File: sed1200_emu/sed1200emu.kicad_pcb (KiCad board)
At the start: 2 copper layers, 114.9 x 36.2 mm, 16 parts, among them CN1 PINHD-1X6, CN2 PINHD-1X6, IC1 MEGA8-AI, Q1 CRYSTALHC49S

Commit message: Update PCB
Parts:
- moved MOSI1 45.8 mm to (153.7, 105.4)
- moved PGND2 16.6 mm to (151.8, 115.6)
- moved C3 8.52 mm to (175.3, 121.3)
- moved C4 7.65 mm to (170.8, 121.3)
- moved C1 4.02 mm to (175.9, 118.7)
- moved C2 2.01 mm to (174.0, 104.8)
- moved R6 1.42 mm to (169.5, 118.7), turned to 180 degrees
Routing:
- net VCC: track 18.2 -> 25.8 mm
- net /RS: track 27.0 -> 22.1 mm
- net Net-(C4-Pad2): track 14.8 -> 9.89 mm
- net /D0: track 38.8 -> 35.4 mm
- net Net-(DIS2-Pad3): track 3.12 -> 0.00 mm
- net Net-(C3-Pad2): track 17.0 -> 13.9 mm
- net Net-(DIS2-Pad6): track 11.2 -> 9.08 mm
- net /D2: track 32.9 -> 31.3 mm
- net /E: track 32.6 -> 31.3 mm

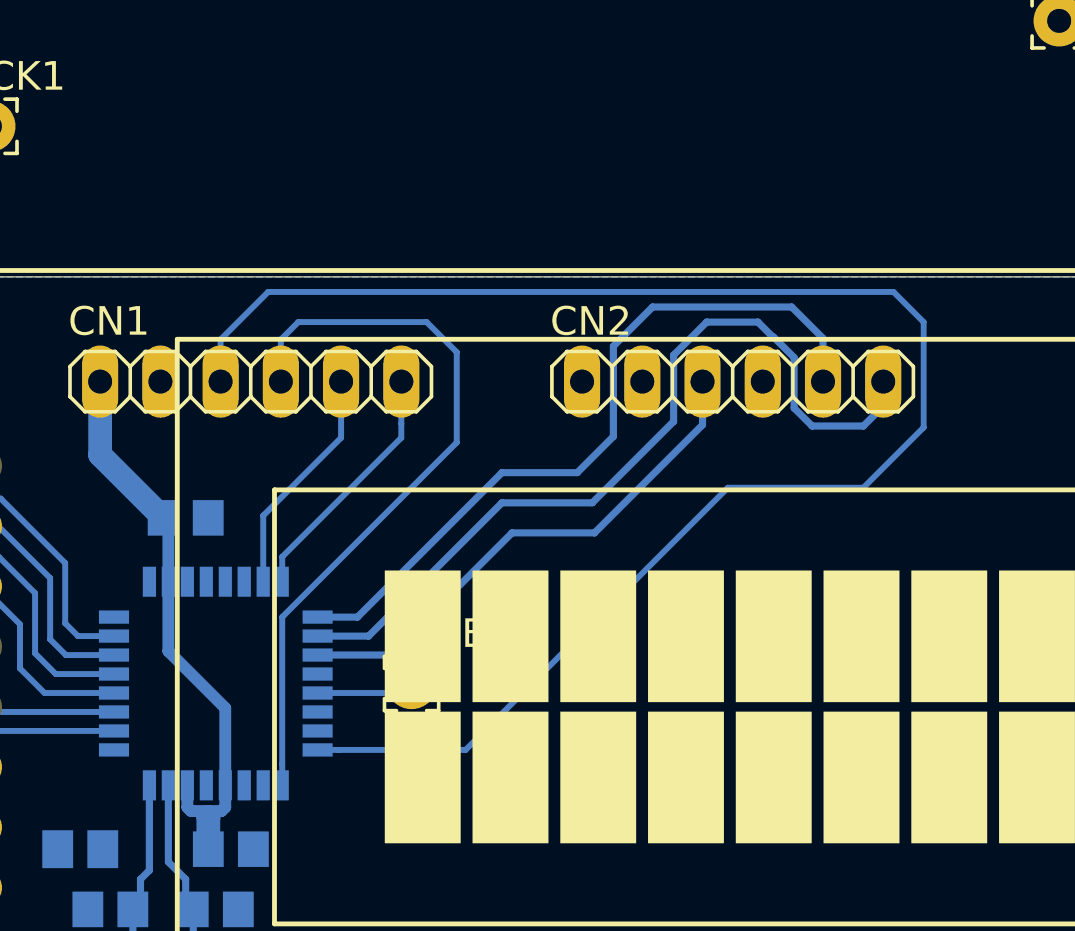
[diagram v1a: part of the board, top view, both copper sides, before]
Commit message: More SMD pads
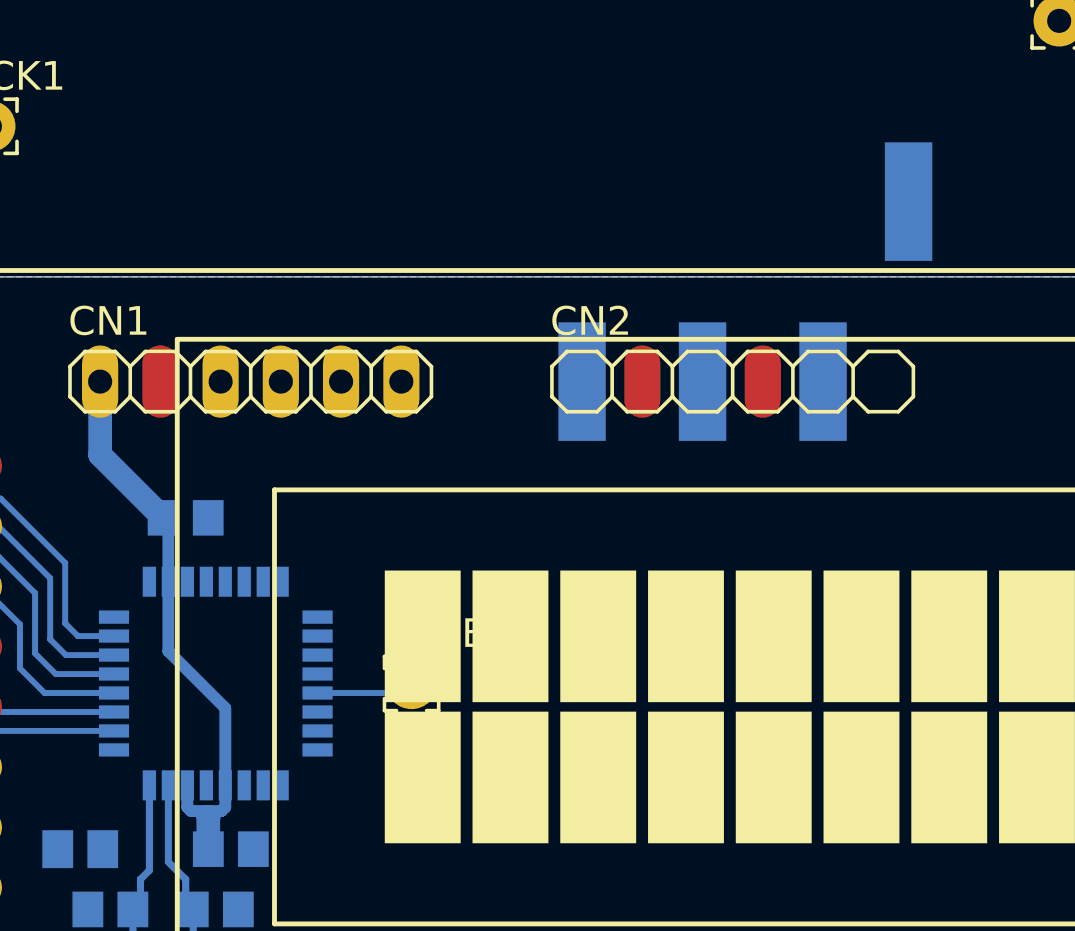
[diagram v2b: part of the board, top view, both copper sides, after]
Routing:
- net /SO_6: track 68.4 -> 0.00 mm
- net /D0: track 35.4 -> 0.00 mm
- net /E: track 31.3 -> 0.00 mm
- net /D2: track 31.3 -> 0.00 mm
- net /RS: track 22.1 -> 0.00 mm
- net /D1: track 10.5 -> 0.00 mm
- net /D3: track 9.80 -> 0.00 mm
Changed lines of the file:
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@@
     (thickness 1.6)
     (drawings 4)
-    (tracks 120)
+    (tracks 66)
     (zones 0)
     (modules 16)
@@
     (mod_text_size 1 1)
     (mod_text_width 0.15)
-    (pad_size 1.6764 1.6764)
+    (pad_size 5 2)
     (pad_drill 0)
     (pad_to_mask_clearance 0.051)
@@
     (fp_line (start 1.905 -1.27) (end 2.54 -0.635) (layer F.SilkS) (width 0.1524))
     (fp_line (start 0.635 -1.27) (end 1.905 -1.27) (layer F.SilkS) (width 0.1524))
-    (pad 6 thru_hole oval (at 6.35 0 90) (size 3.048 1.524) (drill 1.016) (layers *.Cu *.Mask)
+    (pad 1-6 thru_hole oval (at 6.35 0 90) (size 3.048 1.524) (drill 1.016) (layers *.Cu *.Mask)
       (net 5 /D1) (solder_mask_margin 0.1016))
-    (pad 5 thru_hole oval (at 3.81 0 90) (size 3.048 1.524) (drill 1.016) (layers *.Cu *.Mask)
+    (pad 1-5 thru_hole oval (at 3.81 0 90) (size 3.048 1.524) (drill 1.016) (layers *.Cu *.Mask)
       (net 6 /D3) (solder_mask_margin 0.1016))
-    (pad 4 thru_hole oval (at 1.27 0 90) (size 3.048 1.524) (drill 1.016) (layers *.Cu *.Mask)
+    (pad 1-4 thru_hole oval (at 1.27 0 90) (size 3.048 1.524) (drill 1.016) (layers *.Cu *.Mask)
       (net 7 /E) (solder_mask_margin 0.1016))
-    (pad 3 thru_hole oval (at -1.27 0 90) (size 3.048 1.524) (drill 1.016) (layers *.Cu *.Mask)
+    (pad 1-3 thru_hole oval (at -1.27 0 90) (size 3.048 1.524) (drill 1.016) (layers *.Cu *.Mask)
       (net 8 /SO_6) (solder_mask_margin 0.1016))
-    (pad 2 thru_hole oval (at -3.81 0 90) (size 3.048 1.524) (drill 1.016) (layers *.Cu *.Mask)
+    (pad 2 connect oval (at -3.81 0 90) (size 3.048 1.524) (layers Top F.Mask)
       (net 9 "Net-(CN1-Pad2)") (solder_mask_margin 0.1016))
-    (pad 1 thru_hole oval (at -6.35 0 90) (size 3.048 1.524) (drill 1.016) (layers *.Cu *.Mask)
+    (pad 1-1 thru_hole oval (at -6.35 0 90) (size 3.048 1.524) (drill 1.016) (layers *.Cu *.Mask)
       (net 2 VCC) (solder_mask_margin 0.1016))
   )
@@
     (fp_line (start 1.905 -1.27) (end 2.54 -0.635) (layer F.SilkS) (width 0.1524))
     (fp_line (start 0.635 -1.27) (end 1.905 -1.27) (layer F.SilkS) (width 0.1524))
-    (pad 6 thru_hole oval (at 6.35 0 90) (size 3.048 1.524) (drill 1.016) (layers *.Cu *.Mask)
+    (pad 2-6 smd rect (at 7.4169 -7.5896 270) (size 5 2) (layers Bottom B.Paste B.Mask)
       (net 10 /D0) (solder_mask_margin 0.1016))
-    (pad 5 thru_hole oval (at 3.81 0 90) (size 3.048 1.524) (drill 1.016) (layers *.Cu *.Mask)
+    (pad 2-5 smd rect (at 3.81 0 270) (size 5 2) (layers Bottom B.Paste B.Mask)
       (net 11 /D2) (solder_mask_margin 0.1016))
-    (pad 4 thru_hole oval (at 1.27 0 90) (size 3.048 1.524) (drill 1.016) (layers *.Cu *.Mask)
+    (pad 4 connect oval (at 1.27 0 90) (size 3.048 1.524) (layers Top F.Mask)
       (net 12 "Net-(CN2-Pad4)") (solder_mask_margin 0.1016))
-    (pad 3 thru_hole oval (at -1.27 0 90) (size 3.048 1.524) (drill 1.016) (layers *.Cu *.Mask)
+    (pad 2-3 smd rect (at -1.27 0 270) (size 5 2) (layers Bottom B.Paste B.Mask)
       (net 13 /RS) (solder_mask_margin 0.1016))
-    (pad 2 thru_hole oval (at -3.81 0 90) (size 3.048 1.524) (drill 1.016) (layers *.Cu *.Mask)
+    (pad 2 connect oval (at -3.81 0 90) (size 3.048 1.524) (layers Top F.Mask)
       (net 14 "Net-(CN2-Pad2)") (solder_mask_margin 0.1016))
-    (pad 1 thru_hole oval (at -6.35 0 90) (size 3.048 1.524) (drill 1.016) (layers *.Cu *.Mask)
+    (pad 2-1 smd rect (at -6.35 0 90) (size 5 2) (layers Bottom F.Paste F.Mask)
       (net 1 GND) (solder_mask_margin 0.1016))
   )
@@
   (segment (start 171.765 124.145) (end 171.45 124.46) (width 0.3) (layer Bottom) (net 4))
   (segment (start 171.765 121.285) (end 171.765 124.145) (width 0.3) (layer Bottom) (net 4))
-  (segment (start 183.0831 100.8036) (end 183.0831 99.0296) (width 0.25) (layer Bottom) (net 5))
-  (segment (start 183.0831 101.3969) (end 183.0831 100.8036) (width 0.25) (layer Bottom) (net 5))
-  (segment (start 178.06 107.4674) (end 178.06 106.42) (width 0.25) (layer Bottom) (net 5))
-  (segment (start 178.06 106.42) (end 183.0831 101.3969) (width 0.25) (layer Bottom) (net 5))
-  (segment (start 180.5431 101.3969) (end 180.5431 99.0296) (width 0.25) (layer Bottom) (net 6))
-  (segment (start 177.26 107.4674) (end 177.26 104.68) (width 0.25) (layer Bottom) (net 6))
-  (segment (start 177.26 104.68) (end 180.5431 101.3969) (width 0.25) (layer Bottom) (net 6))
-  (segment (start 178.06 115.1676) (end 178.06 116.0526) (width 0.25) (layer Bottom) (net 7))
-  (segment (start 178.06 108.95859) (end 178.06 115.1676) (width 0.25) (layer Bottom) (net 7))
-  (segment (start 185.42 101.59859) (end 178.06 108.95859) (width 0.25) (layer Bottom) (net 7))
-  (segment (start 178.0031 97.2556) (end 178.7387 96.52) (width 0.25) (layer Bottom) (net 7))
-  (segment (start 178.0031 99.0296) (end 178.0031 97.2556) (width 0.25) (layer Bottom) (net 7))
-  (segment (start 184.15 96.52) (end 185.42 97.79) (width 0.25) (layer Bottom) (net 7))
-  (segment (start 178.7387 96.52) (end 184.15 96.52) (width 0.25) (layer Bottom) (net 7))
-  (segment (start 185.42 97.79) (end 185.42 101.59859) (width 0.25) (layer Bottom) (net 7))
-  (segment (start 180.4376 114.56) (end 179.5526 114.56) (width 0.25) (layer Bottom) (net 8))
-  (segment (start 185.795 114.56) (end 180.4376 114.56) (width 0.25) (layer Bottom) (net 8))
-  (segment (start 196.85 103.505) (end 185.795 114.56) (width 0.25) (layer Bottom) (net 8))
-  (segment (start 202.565 103.505) (end 196.85 103.505) (width 0.25) (layer Bottom) (net 8))
-  (segment (start 205.105 100.965) (end 202.565 103.505) (width 0.25) (layer Bottom) (net 8))
-  (segment (start 175.4631 97.2556) (end 177.4687 95.25) (width 0.25) (layer Bottom) (net 8))
-  (segment (start 175.4631 99.0296) (end 175.4631 97.2556) (width 0.25) (layer Bottom) (net 8))
-  (segment (start 177.4687 95.25) (end 203.835 95.25) (width 0.25) (layer Bottom) (net 8))
-  (segment (start 203.835 95.25) (end 205.105 96.52) (width 0.25) (layer Bottom) (net 8))
-  (segment (start 205.105 96.52) (end 205.105 100.965) (width 0.25) (layer Bottom) (net 8))
-  (segment (start 203.4031 100.06551) (end 203.4031 99.0296) (width 0.3) (layer Bottom) (net 10))
-  (segment (start 202.565 100.90361) (end 203.4031 100.06551) (width 0.3) (layer Bottom) (net 10))
-  (segment (start 200.402491 100.90361) (end 202.565 100.90361) (width 0.3) (layer Bottom) (net 10))
-  (segment (start 199.644 100.145119) (end 200.402491 100.90361) (width 0.3) (layer Bottom) (net 10))
-  (segment (start 194.564 100.711) (end 194.564 97.914081) (width 0.3) (layer Bottom) (net 10))
-  (segment (start 191.135 104.14) (end 194.564 100.711) (width 0.3) (layer Bottom) (net 10))
-  (segment (start 187.325 104.14) (end 191.135 104.14) (width 0.3) (layer Bottom) (net 10))
-  (segment (start 179.5526 109.76) (end 181.705 109.76) (width 0.3) (layer Bottom) (net 10))
-  (segment (start 181.705 109.76) (end 187.325 104.14) (width 0.3) (layer Bottom) (net 10))
-  (segment (start 194.564 97.914081) (end 195.958081 96.52) (width 0.3) (layer Bottom) (net 10))
-  (segment (start 195.958081 96.52) (end 198.12 96.52) (width 0.3) (layer Bottom) (net 10))
-  (segment (start 198.12 96.52) (end 198.75559 97.15559) (width 0.3) (layer Bottom) (net 10))
-  (segment (start 198.75559 97.15559) (end 198.783709 97.15559) (width 0.3) (layer Bottom) (net 10))
-  (segment (start 198.783709 97.15559) (end 199.644 98.015881) (width 0.3) (layer Bottom) (net 10))
-  (segment (start 199.644 98.015881) (end 199.644 100.145119) (width 0.3) (layer Bottom) (net 10))
-  (segment (start 200.8631 97.2056) (end 200.8631 99.0296) (width 0.3) (layer Bottom) (net 11))
-  (segment (start 199.5425 95.885) (end 200.8631 97.2056) (width 0.3) (layer Bottom) (net 11))
-  (segment (start 193.675 95.885) (end 199.5425 95.885) (width 0.3) (layer Bottom) (net 11))
-  (segment (start 192.024 97.536) (end 193.675 95.885) (width 0.3) (layer Bottom) (net 11))
-  (segment (start 181.235 108.96) (end 187.325 102.87) (width 0.3) (layer Bottom) (net 11))
-  (segment (start 179.5526 108.96) (end 181.235 108.96) (width 0.3) (layer Bottom) (net 11))
-  (segment (start 187.325 102.87) (end 190.5 102.87) (width 0.3) (layer Bottom) (net 11))
-  (segment (start 190.5 102.87) (end 192.024 101.346) (width 0.3) (layer Bottom) (net 11))
-  (segment (start 192.024 101.346) (end 192.024 97.536) (width 0.3) (layer Bottom) (net 11))
-  (segment (start 195.7831 100.8536) (end 195.7831 99.0296) (width 0.3) (layer Bottom) (net 13))
-  (segment (start 191.2267 105.41) (end 195.7831 100.8536) (width 0.3) (layer Bottom) (net 13))
-  (segment (start 182.599338 110.56) (end 187.749338 105.41) (width 0.3) (layer Bottom) (net 13))
-  (segment (start 187.749338 105.41) (end 191.2267 105.41) (width 0.3) (layer Bottom) (net 13))
-  (segment (start 179.5526 110.56) (end 182.599338 110.56) (width 0.3) (layer Bottom) (net 13))
   (segment (start 163.703299 104.287401) (end 162.8651 105.1256) (width 0.25) (layer Bottom) (net 17))
   (segment (start 164.028301 103.962399) (end 163.703299 104.287401) (width 0.25) (layer Bottom) (net 17))
